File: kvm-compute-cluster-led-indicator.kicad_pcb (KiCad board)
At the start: 2 copper layers, 70.3 x 35.6 mm, 29 parts, among them J1 TE_1-1734248-5_FLEX, U1 PCA9685BS,118

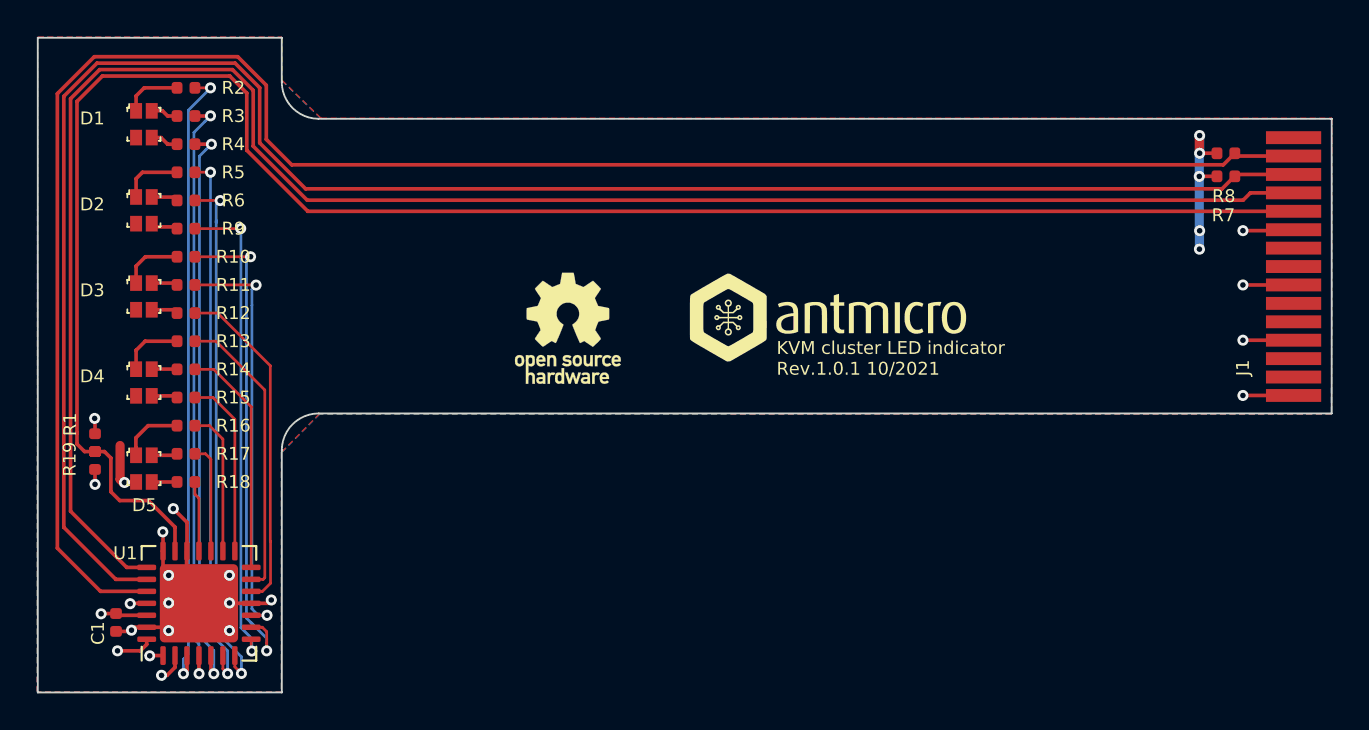
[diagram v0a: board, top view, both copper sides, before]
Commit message: Make flex part thinner
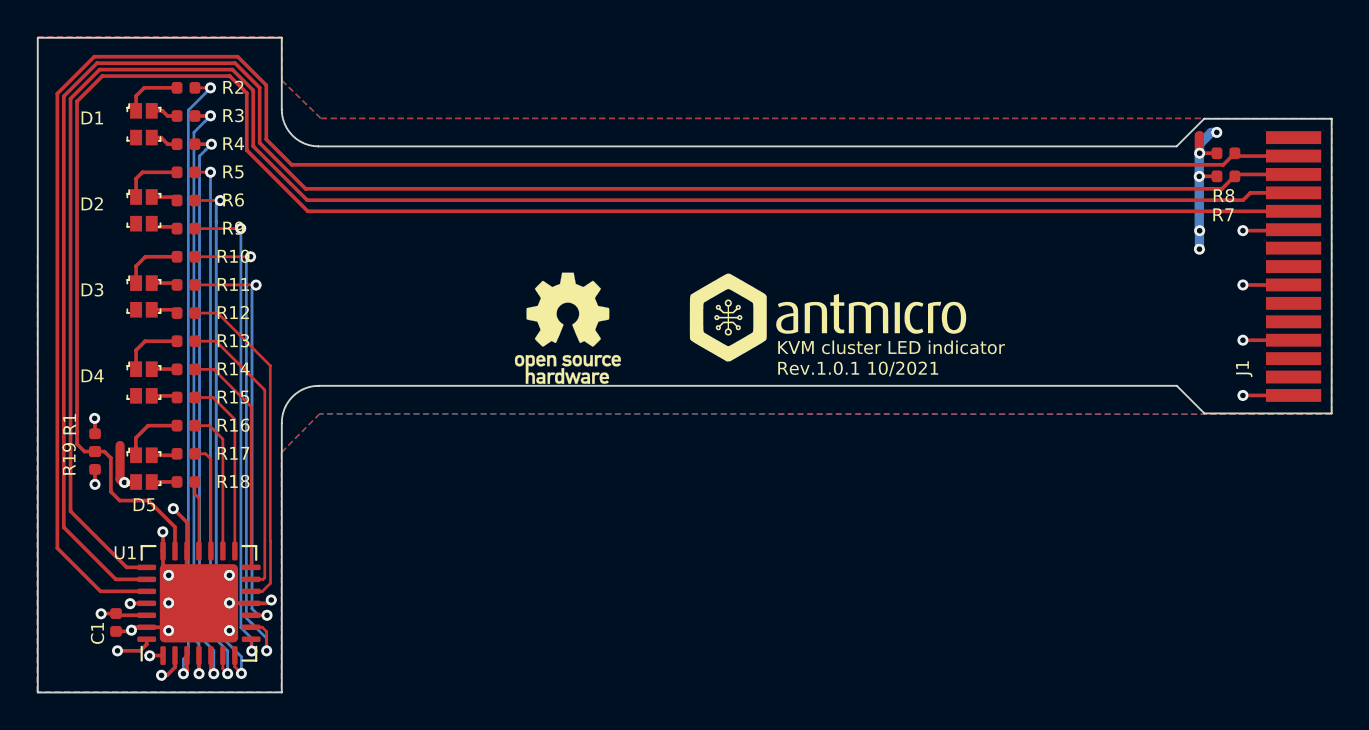
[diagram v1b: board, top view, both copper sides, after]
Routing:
- net +3V3: track 23.9 -> 24.6 mm
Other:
- outline, holes or cut-outs redrawn
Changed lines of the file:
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@@
   (general
     (thickness 0.1)
-    (drawings 219)
-    (tracks 293)
+    (drawings 224)
+    (tracks 295)
     (zones 0)
     (modules 29)
@@
     (31 B.Cu signal)
     (32 B.Adhes user)
-    (33 F.Adhes user)
+    (33 F.Adhes user hide)
     (34 B.Paste user)
     (35 F.Paste user)
@@
     (46 B.CrtYd user hide)
     (47 F.CrtYd user hide)
-    (48 B.Fab user hide)
+    (48 B.Fab user)
     (49 F.Fab user)
   )
@@
     )
   )
+  (gr_line (start 161.259263 115.325849) (end 168.169263 115.325849) (layer Edge.Cuts) (width 0.1))
+  (gr_line (start 161.259263 115.325849) (end 159.759263 113.82585) (layer Edge.Cuts) (width 0.1))
+  (gr_line (start 161.249263 99.32585) (end 168.169263 99.32585) (layer Edge.Cuts) (width 0.1))
+  (gr_line (start 161.249263 99.32585) (end 159.749263 100.82585) (layer Edge.Cuts) (width 0.1))
+  (dimension 35.54996 (width 0.15) (layer Dwgs.User)
+    (gr_text "35.550 mm" (at 91.069185 112.702926 90) (layer Dwgs.User)
+      (effects (font (size 1 1) (thickness 0.15)))
+    )
+    (feature1 (pts (xy 97.91227 130.477257) (xy 91.78445 130.477838)))
+    (feature2 (pts (xy 97.908898 94.927297) (xy 91.781078 94.927878)))
+    (crossbar (pts (xy 92.367499 94.927823) (xy 92.370871 130.477783)))
+    (arrow1a (pts (xy 92.370871 130.477783) (xy 91.784343 129.351335)))
+    (arrow1b (pts (xy 92.370871 130.477783) (xy 92.957185 129.351224)))
+    (arrow2a (pts (xy 92.367499 94.927823) (xy 91.781185 96.054382)))
+    (arrow2b (pts (xy 92.367499 94.927823) (xy 92.954027 96.054271)))
+  )
   (dimension 15.150152 (width 0.15) (layer Dwgs.User)
     (gr_text "15.150 mm" (at 118.166668 122.904181 89.97335678) (layer Dwgs.User)
@@
   (gr_line (start 97.909263 94.93585) (end 97.909263 130.46585) (layer B.Fab) (width 0.15))
   (gr_line (start 111.139263 94.90585) (end 97.909263 94.93585) (layer B.Fab) (width 0.15))
-  (gr_line (start 111.158845 94.92604) (end 111.159263 97.32604) (layer Edge.Cuts) (width 0.1))
+  (gr_line (start 111.158845 94.92604) (end 111.159263 98.82585) (layer Edge.Cuts) (width 0.1))
   (gr_line (start 97.908898 94.927297) (end 111.158845 94.92604) (layer Edge.Cuts) (width 0.1))
   (gr_line (start 168.169263 115.32585) (end 168.169263 99.325851) (layer Edge.Cuts) (width 0.1))
-  (gr_line (start 113.160781 115.325851) (end 168.169263 115.32585) (layer Edge.Cuts) (width 0.1))
-  (gr_line (start 113.149263 99.325827) (end 168.169263 99.325851) (layer Edge.Cuts) (width 0.1))
+  (gr_line (start 113.160781 113.825851) (end 159.759263 113.82585) (layer Edge.Cuts) (width 0.1))
+  (gr_line (start 113.149263 100.825827) (end 159.749263 100.82585) (layer Edge.Cuts) (width 0.1))
   (gr_line (start 102.820086 107.996792) (end 102.820039 107.496792) (layer Margin) (width 0.1))
   (gr_line (start 104.630436 111.693288) (end 104.63046 111.943288) (layer Margin) (width 0.1))
@@
   (gr_line (start 97.91227 130.477257) (end 97.908898 94.927297) (layer Edge.Cuts) (width 0.1))
   (gr_line (start 111.162218 130.476) (end 97.91227 130.477257) (layer Edge.Cuts) (width 0.1))
-  (gr_line (start 111.16097 117.32604) (end 111.162218 130.476) (layer Edge.Cuts) (width 0.1))
-  (gr_arc (start 113.16097 117.325851) (end 113.160781 115.325851) (angle -89.99999995) (layer Edge.Cuts) (width 0.1))
-  (gr_arc (start 113.159073 97.325851) (end 111.159263 97.32585) (angle -89.71896503) (layer Edge.Cuts) (width 0.1))
+  (gr_line (start 111.16097 115.82604) (end 111.162218 130.476) (layer Edge.Cuts) (width 0.1))
+  (gr_arc (start 113.16097 115.825851) (end 113.160781 113.825851) (angle -89.99999995) (layer Edge.Cuts) (width 0.1))
+  (gr_arc (start 113.159073 98.825851) (end 111.159263 98.82585) (angle -89.71896503) (layer Edge.Cuts) (width 0.1))
   (gr_line (start 105.909273 99.436499) (end 106.409273 99.436452) (layer Margin) (width 0.1))
   (gr_line (start 105.90923 98.976499) (end 105.909273 99.436499) (layer Margin) (width 0.1))
@@
   (segment (start 160.98 105.386587) (end 160.999263 105.40585) (width 0.5) (layer B.Cu) (net 6))
   (segment (start 160.98 101.195) (end 160.98 105.386587) (width 0.5) (layer B.Cu) (net 6))
-  (via (at 160.999263 100.23585) (size 0.6) (drill 0.3) (layers F.Cu B.Cu) (net 6))
+  (via (at 161.929263 100.06585) (size 0.6) (drill 0.3) (layers F.Cu B.Cu) (net 6))
   (segment (start 160.98 101.195) (end 160.98 100.255113) (width 0.5) (layer F.Cu) (net 6))
   (segment (start 160.98 100.255113) (end 160.999263 100.23585) (width 0.5) (layer F.Cu) (net 6))
-  (segment (start 160.999263 101.195) (end 160.999263 100.23585) (width 0.5) (layer B.Cu) (net 6))
   (segment (start 160.989263 105.41585) (end 160.999263 105.40585) (width 0.5) (layer B.Cu) (net 6))
   (segment (start 160.989263 106.40585) (end 160.989263 105.41585) (width 0.5) (layer B.Cu) (net 6))
@@
   (segment (start 102.619263 119.07585) (end 102.549263 119.07585) (width 0.5) (layer F.Cu) (net 6))
   (segment (start 102.549263 119.07585) (end 102.379273 118.90586) (width 0.5) (layer F.Cu) (net 6))
+  (segment (start 160.999263 101.195) (end 160.999263 100.69585) (width 0.5) (layer B.Cu) (net 6))
+  (segment (start 161.629263 100.06585) (end 161.929263 100.06585) (width 0.5) (layer B.Cu) (net 6))
+  (segment (start 160.999263 100.69585) (end 161.629263 100.06585) (width 0.5) (layer B.Cu) (net 6))
   (via (at 107.468532 129.4567) (size 0.6) (drill 0.3) (layers F.Cu B.Cu) (net 7))
   (segment (start 106.443526 100.703848) (end 107.335674 100.703848) (width 0.2) (layer F.Cu) (net 7))

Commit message: Move logos
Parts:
- moved N1 1.67 mm to (141.2, 108.5)
- moved N2 1.44 mm to (126.5, 109.3)
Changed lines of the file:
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@@
     (visible_elements 7FFFFFFF)
     (pcbplotparams
-      (layerselection 0x010fc_ffffffff)
-      (usegerberextensions false)
-      (usegerberattributes true)
-      (usegerberadvancedattributes true)
-      (creategerberjobfile true)
+      (layerselection 0x110fc_ffffffff)
+      (usegerberextensions true)
+      (usegerberattributes false)
+      (usegerberadvancedattributes false)
+      (creategerberjobfile false)
       (excludeedgelayer true)
       (linewidth 0.100000)
@@
       (plotvalue true)
       (plotinvisibletext false)
-      (padsonsilk false)
+      (padsonsilk true)
       (subtractmaskfromsilk false)
       (outputformat 1)
       (mirror false)
-      (drillshape 1)
+      (drillshape 0)
       (scaleselection 1)
-      (outputdirectory ""))
+      (outputdirectory "fab/"))
   )
   (net 0 "")
@@
     (pad 1 smd roundrect (at -2.8375 -1.95 90) (size 1.025 0.3) (layers F.Cu F.Paste F.Mask) (roundrect_rratio 0.25)
       (net 22 GND))
-    (pad "" smd roundrect (at 1.42 1.42 90) (size 1.14 1.14) (layers F.Paste) (roundrect_rratio 0.219298))
-    (pad "" smd roundrect (at 1.42 0 90) (size 1.14 1.14) (layers F.Paste) (roundrect_rratio 0.219298))
-    (pad "" smd roundrect (at 1.42 -1.42 90) (size 1.14 1.14) (layers F.Paste) (roundrect_rratio 0.219298))
-    (pad "" smd roundrect (at 0 1.42 90) (size 1.14 1.14) (layers F.Paste) (roundrect_rratio 0.219298))
-    (pad "" smd roundrect (at 0 0 90) (size 1.14 1.14) (layers F.Paste) (roundrect_rratio 0.219298))
-    (pad "" smd roundrect (at 0 -1.42 90) (size 1.14 1.14) (layers F.Paste) (roundrect_rratio 0.219298))
-    (pad "" smd roundrect (at -1.42 1.42 90) (size 1.14 1.14) (layers F.Paste) (roundrect_rratio 0.219298))
-    (pad "" smd roundrect (at -1.42 0 90) (size 1.14 1.14) (layers F.Paste) (roundrect_rratio 0.219298))
-    (pad "" smd roundrect (at -1.42 -1.42 90) (size 1.14 1.14) (layers F.Paste) (roundrect_rratio 0.219298))
+    (pad "" smd roundrect (at 1.42 1.42 90) (size 1.14 1.14) (layers F.Paste) (roundrect_rratio 0.2192973684210526))
+    (pad "" smd roundrect (at 1.42 0 90) (size 1.14 1.14) (layers F.Paste) (roundrect_rratio 0.2192973684210526))
+    (pad "" smd roundrect (at 1.42 -1.42 90) (size 1.14 1.14) (layers F.Paste) (roundrect_rratio 0.2192973684210526))
+    (pad "" smd roundrect (at 0 1.42 90) (size 1.14 1.14) (layers F.Paste) (roundrect_rratio 0.2192973684210526))
+    (pad "" smd roundrect (at 0 0 90) (size 1.14 1.14) (layers F.Paste) (roundrect_rratio 0.2192973684210526))
+    (pad "" smd roundrect (at 0 -1.42 90) (size 1.14 1.14) (layers F.Paste) (roundrect_rratio 0.2192973684210526))
+    (pad "" smd roundrect (at -1.42 1.42 90) (size 1.14 1.14) (layers F.Paste) (roundrect_rratio 0.2192973684210526))
+    (pad "" smd roundrect (at -1.42 0 90) (size 1.14 1.14) (layers F.Paste) (roundrect_rratio 0.2192973684210526))
+    (pad "" smd roundrect (at -1.42 -1.42 90) (size 1.14 1.14) (layers F.Paste) (roundrect_rratio 0.2192973684210526))
     (pad 29 smd roundrect (at 0 0 90) (size 4.25 4.25) (layers F.Cu F.Mask) (roundrect_rratio 0.058824)
       (net 22 GND))
@@
   )
   (module antmicro-footprints:antmicro-logo_scaled_15mm_silk (layer F.Cu)
-    (at 141.27 110.19)
+    (at 141.25 108.52)
     (attr virtual)
     (fp_text reference N1 (at -7.7 -10.3) (layer F.SilkS) hide
@@
   )
   (module antmicro-footprints:OSHW-Logo_5.7x6mm_SilkScreen (layer F.Cu)
-    (at 126.69 110.7)
+    (at 126.509263 109.27585)
     (descr "Open Source Hardware Logo")
     (tags "Logo OSHW")
@@
   (gr_line (start 168.15 99.35) (end 168.15 115.35) (layer B.Fab) (width 0.15))
   (gr_line (start 111.139263 94.90585) (end 111.139263 130.46585) (layer B.Fab) (width 0.15))
-  (gr_text "KVM cluster LED indicator\nRev.1.0.1 10/2021" (at 138.025 112.335) (layer F.SilkS)
+  (gr_text "KVM cluster LED indicator\nRev.1.0.1 10/2021" (at 138.005 110.665) (layer F.SilkS)
     (effects (font (size 0.7 0.7) (thickness 0.15)) (justify left))
   )

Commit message: Add local libraries
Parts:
- C1: footprint antmicro-footprints:0402-cap -> kvm-compute-cluster-led-indicator-footprints:0402-cap
- D1, D2, D3, D4, D5: footprint antmicro-footprints:LED_Dual0603 -> kvm-compute-cluster-led-indicator-footprints:LED_Dual0603
- J1: footprint antmicro-footprints:TE_1-1734248-5_FLEX -> kvm-compute-cluster-led-indicator-footprints:TE_1-1734248-5_FLEX
- N1: footprint antmicro-footprints:antmicro-logo_scaled_15mm_silk -> kvm-compute-cluster-led-indicator-footprints:antmicro-logo_scaled_15mm_silk
- N2: footprint antmicro-footprints:OSHW-Logo_5.7x6mm_SilkScreen -> kvm-compute-cluster-led-indicator-footprints:OSHW-Logo_5.7x6mm_SilkScreen
- R1, R10, R11, R12, R13, R14, R15, R16, R17, R18, R19, R2, R3, R4, R5, R6, R7, R8, R9: footprint antmicro-footprints:0402-res -> kvm-compute-cluster-led-indicator-footprints:0402-res
- U1: footprint antmicro-footprints:QFN-28_6x6mm_P0.65mm -> kvm-compute-cluster-led-indicator-footprints:QFN-28_6x6mm_P0.65mm
